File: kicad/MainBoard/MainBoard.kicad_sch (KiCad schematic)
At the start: 96 parts, among them J1 CHAN1, J10 ACC Port, J11 433TX, J12 VDC INPUT, J13 BAT, J14 TRG1, J15 TRG2, J16 FP-BUTTONS, J17 EXPAN2, J18 OUTPUT_BOARD_POWER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

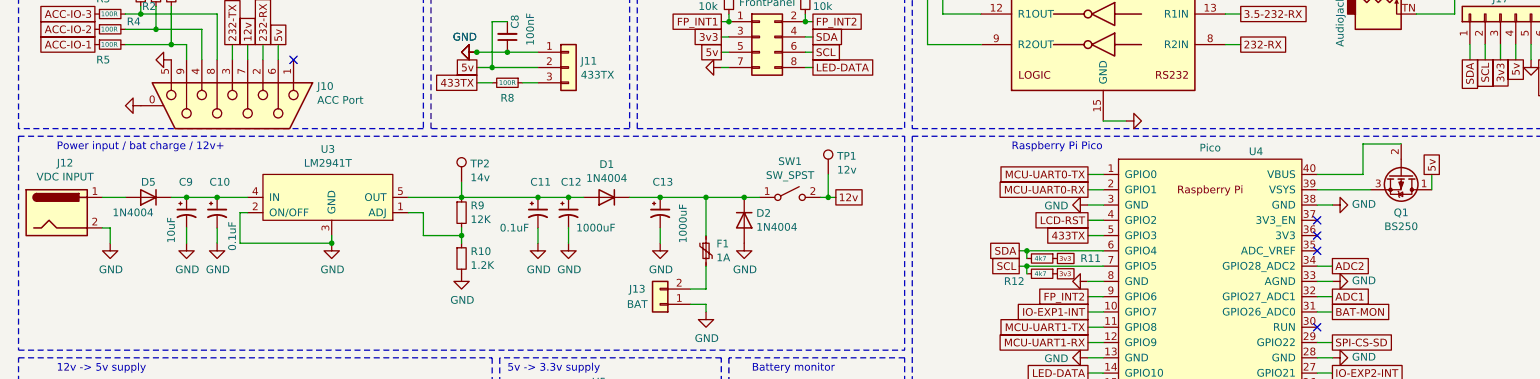
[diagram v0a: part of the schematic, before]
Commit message: Switch Mainboard Q1, D1, D2, D5 with 1N5819
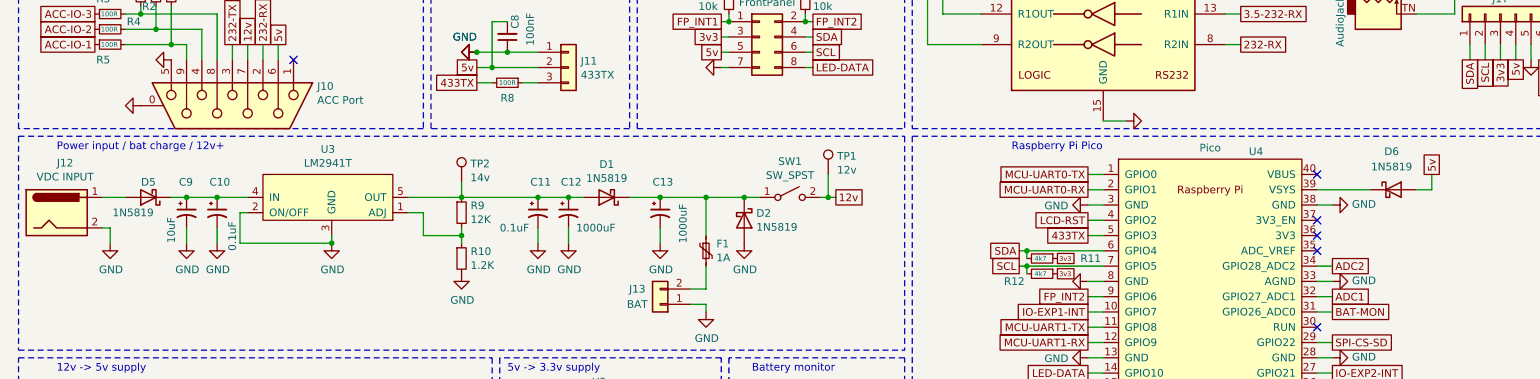
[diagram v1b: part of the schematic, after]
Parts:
- removed Q1: BS250, Package_TO_SOT_THT:TO-92_Inline_Wide, symbol Transistor_FET:BS250
- added D6: 1N5819, Diode_THT:D_DO-41_SOD81_P10.16mm_Horizontal, symbol Diode:1N5819
- D1, D2, D5: value 1N4004 -> 1N5819; symbol Diode:1N4004 -> Diode:1N5819
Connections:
- net 5v: now also D6.2 (A)
- net at U4.39 (VSYS): now also D6.1 (K)
- no-connect marks 29 -> 30
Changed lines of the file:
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@@
 	)
 	(no_connect
+		(at 231.14 87.63)
+	)
+	(no_connect
 		(at 246.38 161.29)
 	)
@@
 	(wire
 		(pts
-			(xy 238.76 87.63) (xy 238.76 82.55)
-		)
-		(stroke
-			(width 0)
-			(type default)
-		)
-	)
-	(wire
-		(pts
 			(xy 261.62 66.04) (xy 261.62 68.58)
 		)
@@
 	(wire
 		(pts
-			(xy 231.14 87.63) (xy 238.76 87.63)
-		)
-		(stroke
-			(width 0)
-			(type default)
-		)
-	)
-	(wire
-		(pts
 			(xy 90.17 172.72) (xy 91.44 172.72)
 		)
@@
 	(wire
 		(pts
+			(xy 247.65 90.17) (xy 250.19 90.17)
+		)
+		(stroke
+			(width 0)
+			(type default)
+		)
+	)
+	(wire
+		(pts
 			(xy 153.67 168.91) (xy 153.67 156.21)
 		)
@@
 	(wire
 		(pts
-			(xy 238.76 82.55) (xy 245.11 82.55)
-		)
-		(stroke
-			(width 0)
-			(type default)
-		)
-	)
-	(wire
-		(pts
 			(xy 120.65 153.67) (xy 120.65 154.94)
 		)
@@
 			)
 		)
-		(property "Description" ""
+		(property "Description" "DC Barrel Jack"
 			(at 21.59 93.98 0)
 			(effects
@@
 	)
 	(symbol
-		(lib_id "Diode:1N4004")
+		(lib_id "Diode:1N5819")
 		(at 113.03 91.44 180)
 		(unit 1)
@@
 			)
 		)
-		(property "Value" "1N4004"
+		(property "Value" "1N5819"
 			(at 113.03 88.265 0)
 			(effects
@@
 			)
 		)
-		(property "Datasheet" "http://www.vishay.com/docs/88503/1n4001.pdf"
+		(property "Datasheet" "http://www.vishay.com/docs/88525/1n5817.pdf"
 			(at 113.03 91.44 0)
 			(effects
@@
 			)
 		)
-		(property "Description" ""
+		(property "Description" "40V 1A Schottky Barrier Rectifier Diode, DO-41"
 			(at 113.03 91.44 0)
 			(effects
@@
 	)
 	(symbol
-		(lib_id "Diode:1N4004")
+		(lib_id "Diode:1N5819")
 		(at 135.89 95.25 270)
 		(unit 1)
@@
 			)
 		)
-		(property "Value" "1N4004"
+		(property "Value" "1N5819"
 			(at 137.8966 96.393 90)
 			(effects
@@
 			)
 		)
-		(property "Datasheet" "http://www.vishay.com/docs/88503/1n4001.pdf"
+		(property "Datasheet" "http://www.vishay.com/docs/88525/1n5817.pdf"
 			(at 135.89 95.25 0)
 			(effects
@@
 			)
 		)
-		(property "Description" ""
+		(property "Description" "40V 1A Schottky Barrier Rectifier Diode, DO-41"
 			(at 135.89 95.25 0)
 			(effects
@@
 	)
 	(symbol
-		(lib_id "Transistor_FET:BS250")
-		(at 245.11 87.63 270)
-		(unit 1)
-		(exclude_from_sim no)
-		(in_bom yes)
-		(on_board yes)
-		(dnp no)
-		(property "Reference" "Q1"
-			(at 245.11 93.98 90)
-			(effects
-				(font
-					(size 1.27 1.27)
-				)
-			)
-		)
-		(property "Value" "BS250"
-			(at 245.11 96.2914 90)
-			(effects
-				(font
-					(size 1.27 1.27)
-				)
-			)
-		)
-		(property "Footprint" "Package_TO_SOT_THT:TO-92_Inline_Wide"
-			(at 243.205 92.71 0)
-			(effects
-				(font
-					(size 1.27 1.27)
-					(italic yes)
-				)
-				(justify left)
-				(hide yes)
-			)
-		)
-		(property "Datasheet" "http://www.vishay.com/docs/70209/70209.pdf"
-			(at 245.11 87.63 0)
-			(effects
-				(font
-					(size 1.27 1.27)
-				)
-				(justify left)
-				(hide yes)
-			)
-		)
-		(property "Description" ""
-			(at 245.11 87.63 0)
-			(effects
-				(font
-					(size 1.27 1.27)
-				)
-				(hide yes)
-			)
-		)
-		(pin "1"
-		)
-		(pin "2"
-		)
-		(pin "3"
-		)
-		(instances
-			(project "MainBoard"
-				(path "/bb925afc-cc5a-4bd1-9a37-475961f43ead"
-					(reference "Q1")
-					(unit 1)
-				)
-			)
-		)
-	)
-	(symbol
 		(lib_id "power:GND")
 		(at 233.68 92.71 90)
@@
 	)
 	(symbol
-		(lib_id "Diode:1N4004")
+		(lib_id "Diode:1N5819")
 		(at 36.83 91.44 180)
 		(unit 1)
@@
 			)
 		)
-		(property "Value" "1N4004"
+		(property "Value" "1N5819"
 			(at 34.29 93.98 0)
 			(effects
@@
 			)
 		)
-		(property "Datasheet" "http://www.vishay.com/docs/88503/1n4001.pdf"
+		(property "Datasheet" "http://www.vishay.com/docs/88525/1n5817.pdf"
 			(at 36.83 91.44 0)
 			(effects
@@
 			)
 		)
-		(property "Description" ""
+		(property "Description" "40V 1A Schottky Barrier Rectifier Diode, DO-41"
+			(at 36.83 91.44 0)
+			(effects
+				(font
+					(size 1.27 1.27)
+				)
+				(hide yes)
+			)
+		)
+		(property "Sim.Device" "D"
+			(at 36.83 91.44 0)
+			(effects
+				(font
+					(size 1.27 1.27)
+				)
+				(hide yes)
+			)
+		)
+		(property "Sim.Pins" "1=K 2=A"
 			(at 36.83 91.44 0)
 			(effects
@@
 					(unit 1)
 				)
+			)
+		)
+	)
+	(symbol
+		(lib_id "Diode:1N5819")
+		(at 243.84 90.17 0)
+		(unit 1)
+		(exclude_from_sim no)
+		(in_bom yes)
+		(on_board yes)
+		(dnp no)
+		(fields_autoplaced yes)
+		(property "Reference" "D6"
+			(at 243.5225 83.82 0)
+			(effects
+				(font
+					(size 1.27 1.27)
+				)
+			)
+		)
+		(property "Value" "1N5819"
+			(at 243.5225 86.36 0)
+			(effects
+				(font
+					(size 1.27 1.27)
+				)
+			)
+		)
+		(property "Footprint" "Diode_THT:D_DO-41_SOD81_P10.16mm_Horizontal"
+			(at 243.84 94.615 0)
+			(effects
+				(font
+					(size 1.27 1.27)
+				)
+				(hide yes)
+			)
+		)
+		(property "Datasheet" "http://www.vishay.com/docs/88525/1n5817.pdf"
+			(at 243.84 90.17 0)
+			(effects
+				(font
+					(size 1.27 1.27)
+				)
+				(hide yes)
+			)
+		)
+		(property "Description" "40V 1A Schottky Barrier Rectifier Diode, DO-41"
+			(at 243.84 90.17 0)
+			(effects
+				(font
+					(size 1.27 1.27)
+				)
+				(hide yes)
+			)
+		)
+		(pin "2"
+		)
+		(pin "1"
+		)
+		(instances
+			(project "MainBoard"
+				(path "/bb925afc-cc5a-4bd1-9a37-475961f43ead"
+					(reference "D6")
+					(unit 1)
+				)

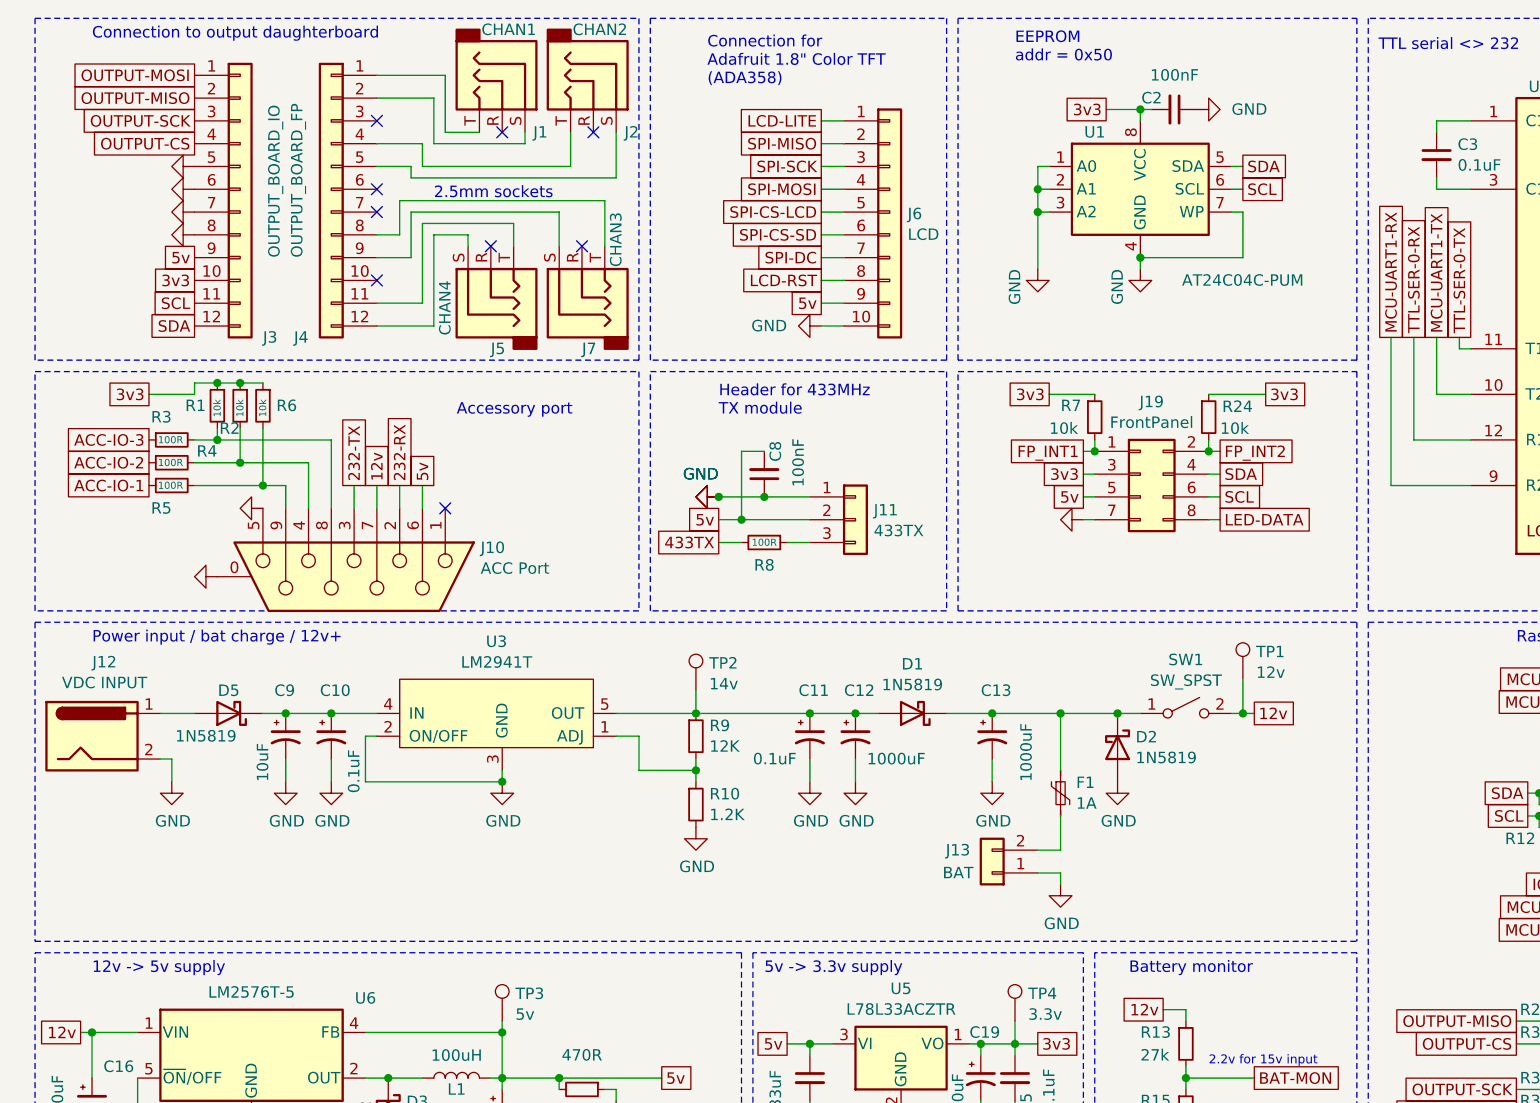
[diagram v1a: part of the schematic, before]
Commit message: Add header for RS232 configuration
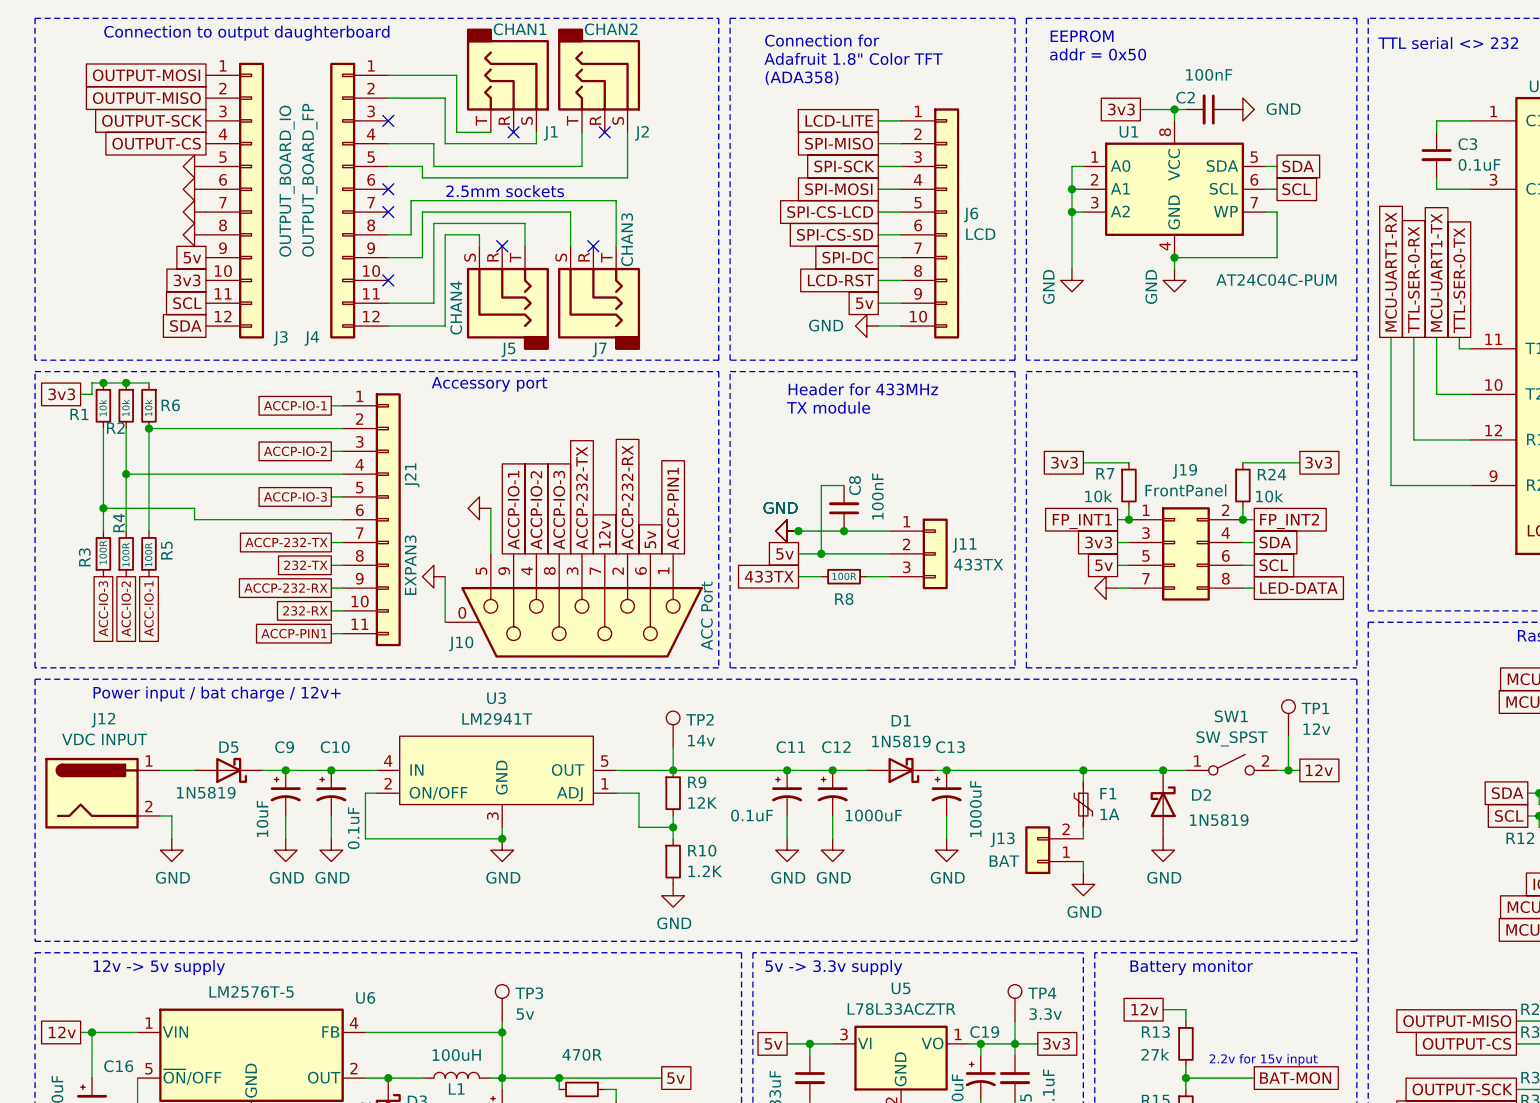
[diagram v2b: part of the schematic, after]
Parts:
- added J21: EXPAN3, Connector_PinSocket_2.54mm:PinSocket_1x11_P2.54mm_Vertical, symbol Connector_Generic:Conn_01x11
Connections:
- net 232-RX: now also J21.10 (Pin_10); no longer J10.2
- net 232-TX: now also J21.8 (Pin_8); no longer J10.3
- net ACCP-PIN1: now reaches J10.1
- net ACCP-PIN1: now also J21.11 (Pin_11)
- net at R2.2, R4.2: now also J21.4 (Pin_4); no longer J10.4
- net at R1.2, R3.2: now also J21.6 (Pin_6); no longer J10.8
- net at R5.2, R6.2: now also J21.2 (Pin_2); no longer J10.9
- new net ACCP-232-RX: J10.2, J21.9 (Pin_9)
- new net ACCP-232-TX: J10.3, J21.7 (Pin_7)
- new net ACCP-IO-1: J10.9, J21.1 (Pin_1)
- new net ACCP-IO-2: J10.4, J21.3 (Pin_3)
- new net ACCP-IO-3: J10.8, J21.5 (Pin_5)
- no-connect marks 30 -> 29
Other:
- moved on the sheet: C10, C11, C12, C13, C2, C8, C9, D1, D2, D5, F1, J1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

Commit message: Before 3.5mm footprint switch
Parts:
- removed J1: CHAN1, ProjLib:PJ-2100B-4A, symbol MainBoard-rescue:AudioJack3-Connector
- removed J2: CHAN2, ProjLib:PJ-2100B-4A, symbol MainBoard-rescue:AudioJack3-Connector
- removed J5: CHAN4, ProjLib:PJ-2100B-4A, symbol MainBoard-rescue:AudioJack3-Connector
- removed J7: CHAN3, ProjLib:PJ-2100B-4A, symbol MainBoard-rescue:AudioJack3-Connector
- added J1, J2: CHAN1, ProjLib:PJ-3062-CO, symbol MainBoard-rescue:AudioJack3_SwitchTR-Connector
- added J5: CHAN4, ProjLib:PJ-3062-CO, symbol MainBoard-rescue:AudioJack3_SwitchTR-Connector
- added J7: CHAN3, ProjLib:PJ-3062-CO, symbol MainBoard-rescue:AudioJack3_SwitchTR-Connector
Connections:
- net at J4.1 (Pin_1): now also J1.R, J1.T
- net at J4.11 (Pin_11): now also J5.R, J5.T
- net at J4.12 (Pin_12): now also J5.S
- net at J4.2 (Pin_2): now also J1.S
- net at J4.4 (Pin_4): now also J2.R, J2.T
- net at J4.5 (Pin_5): now also J2.S
- net at J4.8 (Pin_8): now also J7.R, J7.T
- net at J4.9 (Pin_9): now also J7.S
- no-connect marks 29 -> 33
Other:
- note removed: "2.5mm sockets"
- moved on the sheet: J3, J4

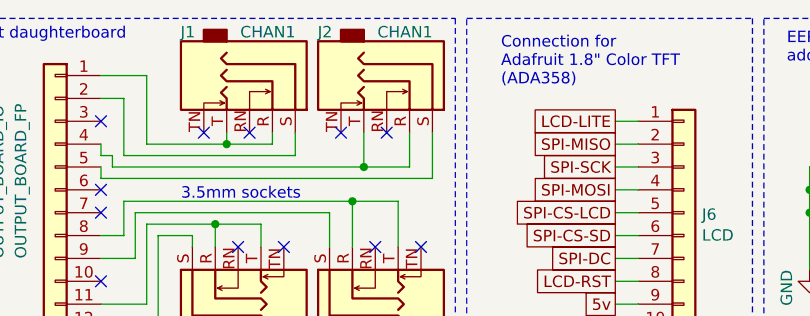
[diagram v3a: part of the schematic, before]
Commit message: Switch everything to 3.5mm plugs
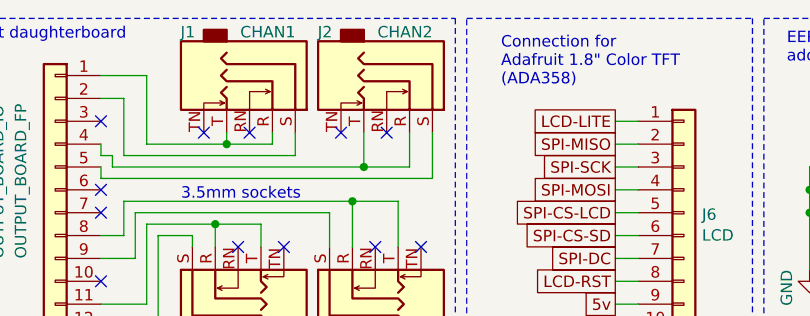
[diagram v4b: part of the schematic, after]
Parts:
- J1, J14, J15, J5, J7, J9: footprint ProjLib:PJ-3062-CO -> ProjLib:STX31005N
- J2: value CHAN1 -> CHAN2; footprint ProjLib:PJ-3062-CO -> ProjLib:STX31005N
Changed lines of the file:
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@@
 			)
 		)
-		(property "Footprint" "ProjLib:PJ-3062-CO"
+		(property "Footprint" "ProjLib:STX31005N"
 			(at 242.57 53.34 0)
 			(effects
@@
 			)
 		)
-		(property "Footprint" "ProjLib:PJ-3062-CO"
+		(property "Footprint" "ProjLib:STX31005N"
 			(at 138.43 173.99 0)
 			(effects
@@
 			)
 		)
-		(property "Footprint" "ProjLib:PJ-3062-CO"
+		(property "Footprint" "ProjLib:STX31005N"
 			(at 156.21 173.99 0)
 			(effects
@@
 			)
 		)
-		(property "Value" "CHAN1"
+		(property "Value" "CHAN2"
 			(at 85.852 15.494 90)
 			(effects
@@
 			)
 		)
-		(property "Footprint" "ProjLib:PJ-3062-CO"
+		(property "Footprint" "ProjLib:STX31005N"
 			(at 86.36 21.59 0)
 			(effects
@@
 			)
 		)
-		(property "Footprint" "ProjLib:PJ-3062-CO"
+		(property "Footprint" "ProjLib:STX31005N"
 			(at 80.01 44.45 0)
 			(effects
@@
 			)
 		)
-		(property "Footprint" "ProjLib:PJ-3062-CO"
+		(property "Footprint" "ProjLib:STX31005N"
 			(at 64.77 44.45 0)
 			(effects
@@
 			)
 		)
-		(property "Footprint" "ProjLib:PJ-3062-CO"
+		(property "Footprint" "ProjLib:STX31005N"
 			(at 71.12 21.59 0)
 			(effects
